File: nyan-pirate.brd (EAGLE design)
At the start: 92.2 x 47.5 mm, 43 parts, among them IC1 PIC24FJ64GA002, IC2 FT232RL, IC3 4066, J1 CON-USB-MINI-BUSB1

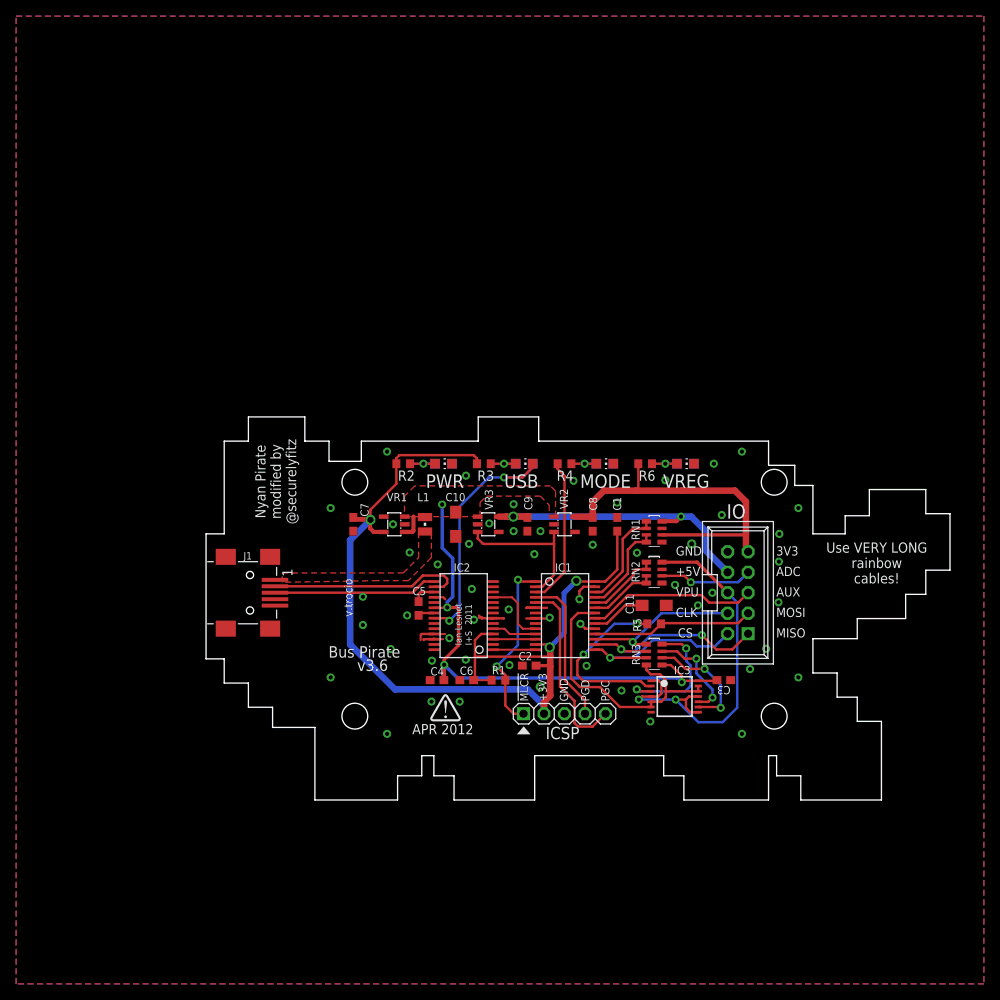
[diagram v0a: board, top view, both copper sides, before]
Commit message: changes to make special Bsides PDX 2014 version
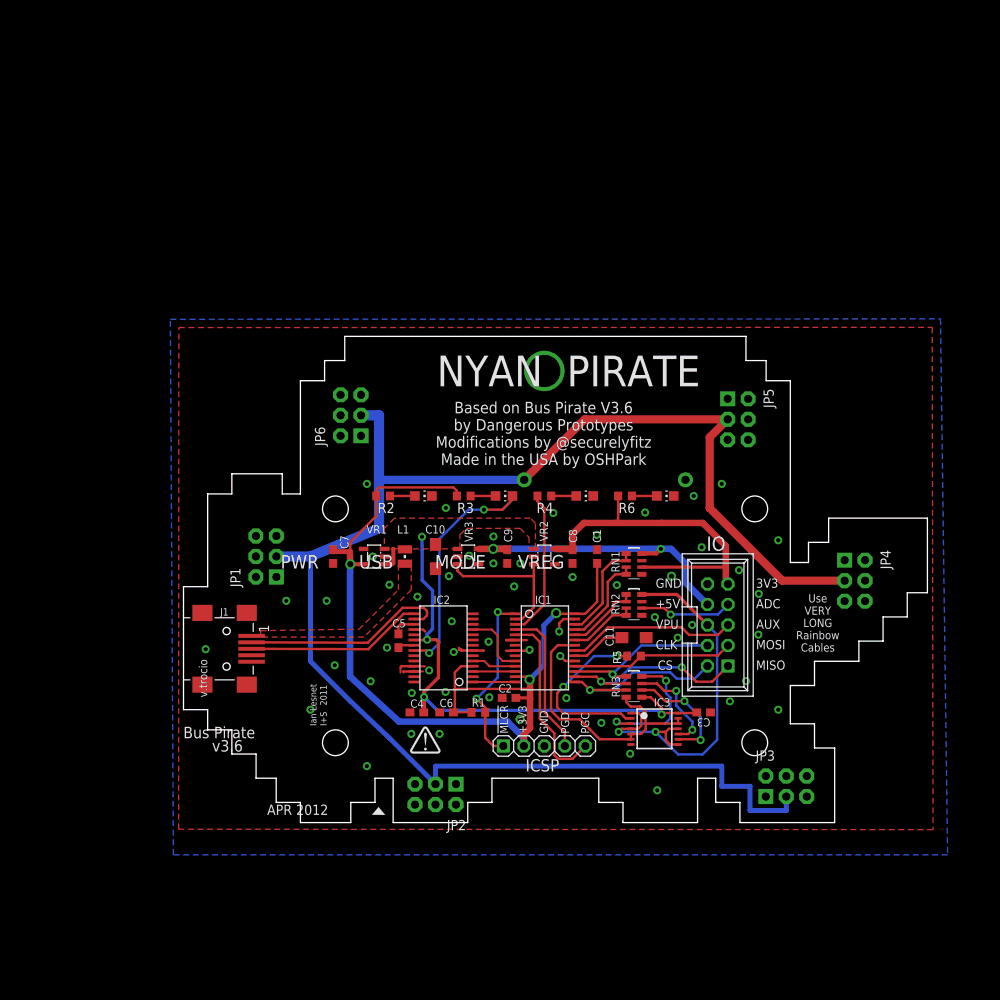
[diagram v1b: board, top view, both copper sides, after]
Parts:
- removed LED1A, LED2A, LED3A, LED4A: (no value), led:CHIP-LED0805
- added 3V, GND: M01NOSILK-KIT, SparkFun-Connectors:1X01NS-KIT
- added JP1, JP2, JP3, JP4, JP5, JP6: (no value), SparkFun-Connectors:2X3-NS
- added U$4: (no value), bsides:BSIDESPDXLOGO3
- PCB1: value PCB_DP_RECTANGLENYAN_PIRATE -> PCB_DP_RECTANGLEBSIDES2014; device dp_pcb:NYAN_PIRATE -> dp_pcb:BIDESPDX2014
- moved PCB1 16.9 mm to (15.5, 6.00)
- moved J1 7.53 mm to (6.10, 21.6)
- moved LOGO1 4.72 mm to (32.0, 14.6)
- moved C1 4.72 mm to (52.0, 33.0)
- moved C10 4.72 mm to (32.0, 33.0)
- moved C11 4.72 mm to (56.6, 22.9)
- moved C2 4.72 mm to (41.1, 15.5)
- moved C5 4.72 mm to (27.4, 22.6)
- moved C7 4.72 mm to (19.3, 33.0)
- moved C8 4.72 mm to (49.0, 33.0)
- moved C9 4.72 mm to (40.9, 33.0)
- moved IC1 4.72 mm to (45.6, 21.7)
- moved IC2 4.72 mm to (33.0, 21.7)
- moved IC3 4.72 mm to (59.2, 11.6)
- moved ICSP 4.72 mm to (45.5, 9.50)
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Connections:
- new net N$10: JP2.2, JP2.4, JP2.6
- new net N$11: JP3.2, JP3.4, JP3.6
- new net N$12: JP4.2, JP4.4, JP4.6
- new net N$14: JP5.2, JP5.4, JP5.6
- new net N$17: JP6.2, JP6.4, JP6.6
- new net N$20: 3V.1, JP1.3, JP2.3, JP3.3, JP4.3, JP5.3, JP6.3
- new net N$8: JP1.2, JP1.4, JP1.6
- net GND: now also GND.1, JP1.1, JP1.5, JP2.1, JP2.5, JP3.1, JP3.5, JP4.1, JP4.5, JP5.1, JP5.5, JP6.1, JP6.5; no longer LED1A.C, LED2A.C, LED3A.C
- net N$13: no longer LED4A.A
- net N$18: no longer LED3A.A
- net N$6: no longer LED2A.A
- net N$7: no longer LED1A.A
- net RXLED: no longer LED4A.C
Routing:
- net N$20: track 0.00 -> 196.1 mm
- net VCC: track 122.2 -> 125.8 mm
- net N$16: track 24.4 -> 26.1 mm
- net N$15: track 20.3 -> 22.0 mm
- net N$6: track 4.55 -> 3.10 mm, vias 1 -> 0
- net N$18: track 4.55 -> 3.10 mm, vias 1 -> 0
- net N$13: track 4.55 -> 3.10 mm, vias 1 -> 0
- net N$7: track 4.55 -> 3.10 mm, vias 1 -> 0
- net SWV33: track 44.7 -> 43.8 mm
- net GND: vias 54 -> 56
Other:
- board size 92.2 x 47.5 mm -> 92.2 x 60.3 mm
- board text added: "2014"
- board text added: "Based on Bus Pirate V3.6 by Dangerous Prototypes Modifications by @securelyfitz Made in the USA by OSHPark"
- board text added: "Made in the USA by OSHPark"
- board text added: "Use VERY LONG Rainbow Cables"
- board text removed: "Nyan Pirate modified by @securelyfitz"
- board text removed: "Programming Header"
- board text removed: "Use VERY LONG rainbow cables!"
